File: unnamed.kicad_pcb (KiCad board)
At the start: 2 copper layers, 140 x 95 mm, 29 parts, among them J1 C128990, J2 C128990, SW1 KeySwitch, SW10 KeySwitch, SW11 KeySwitch, SW12 KeySwitch, SW13 KeySwitch, SW14 KeySwitch, SW15 KeySwitch, SW16 KeySwitch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

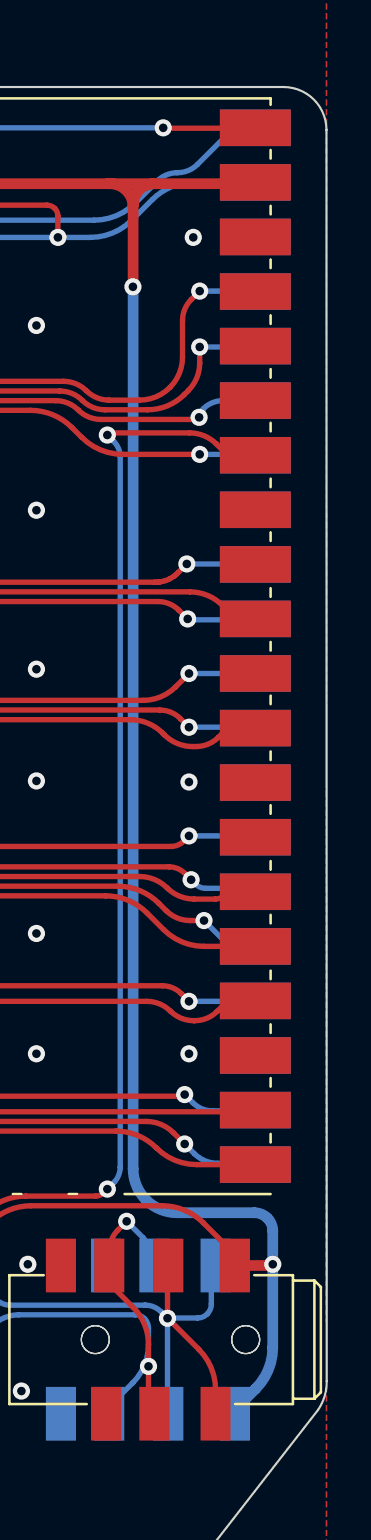
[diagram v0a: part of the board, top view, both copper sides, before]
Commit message: update pcb with edge modification a little bit. add case
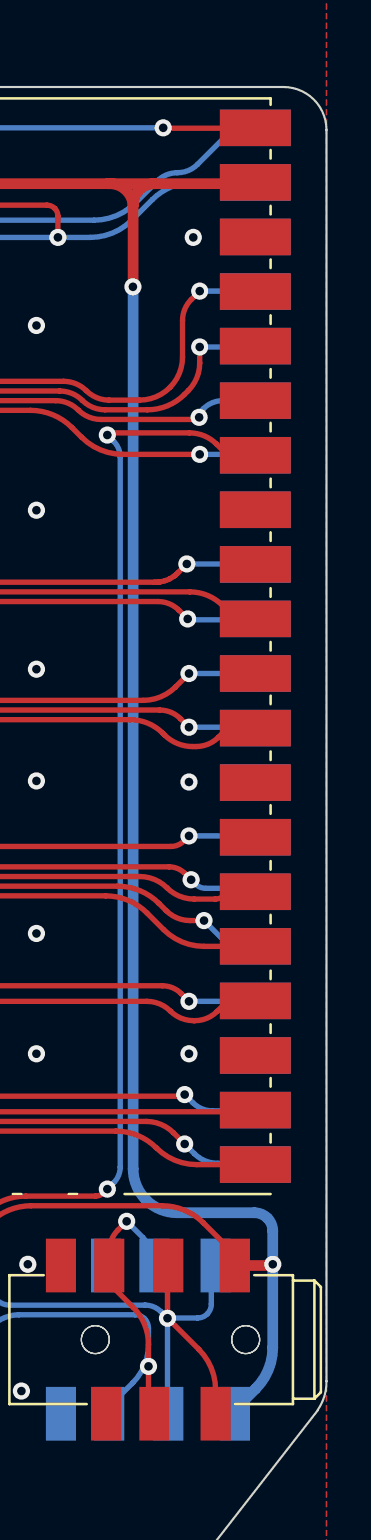
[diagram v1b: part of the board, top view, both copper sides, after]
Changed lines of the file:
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@@
     (aux_axis_origin 80 50)
     (pcbplotparams
-      (layerselection 0x0001020_7ffffffe)
+      (layerselection 0x0001000_7ffffffe)
       (plot_on_all_layers_selection 0x0001000_00000000)
       (disableapertmacros false)
@@
   (gr_arc (start 154.8 50) (mid 156.214214 50.585786) (end 156.8 52)
     (stroke (width 0.1) (type solid)) (layer "Edge.Cuts"))
-  (gr_arc (start 220.0114 118.237) (mid 219.913988 118.942037) (end 219.605 119.5832)
+  (gr_arc (start 219.999999 118.237) (mid 219.903102 118.938639) (end 219.59562 119.576714)
     (stroke (width 0.1) (type solid)) (layer "Edge.Cuts"))
   (gr_line (start 80 62) (end 80 118)
@@
   (gr_arc (start 158.8 55) (mid 157.385786 54.414214) (end 156.8 53)
     (stroke (width 0.1) (type solid)) (layer "Edge.Cuts"))
-  (gr_line (start 220 60) (end 220.0114 118.237)
+  (gr_line (start 220 60) (end 220 118.237)
     (stroke (width 0.1) (type solid)) (layer "Edge.Cuts"))
   (gr_arc (start 173.800001 54.99997) (mid 174.953205 55.446145) (end 175.599999 56.5)
